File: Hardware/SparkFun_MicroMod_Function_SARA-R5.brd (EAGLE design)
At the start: 37.5 x 65 mm, 120 parts, among them J1 MICROMOD_FUNCTION_STANDARD, J2 U.FL, J4 U.FL, J9 NANO_SIM, Q2 310mA/60V/1.6Ω, Q3 310mA/60V/1.6Ω, Q5 310mA/60V/1.6Ω, Q6 310mA/60V/1.6Ω, U1 SARA-R510M8S, U11 74HC1G04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

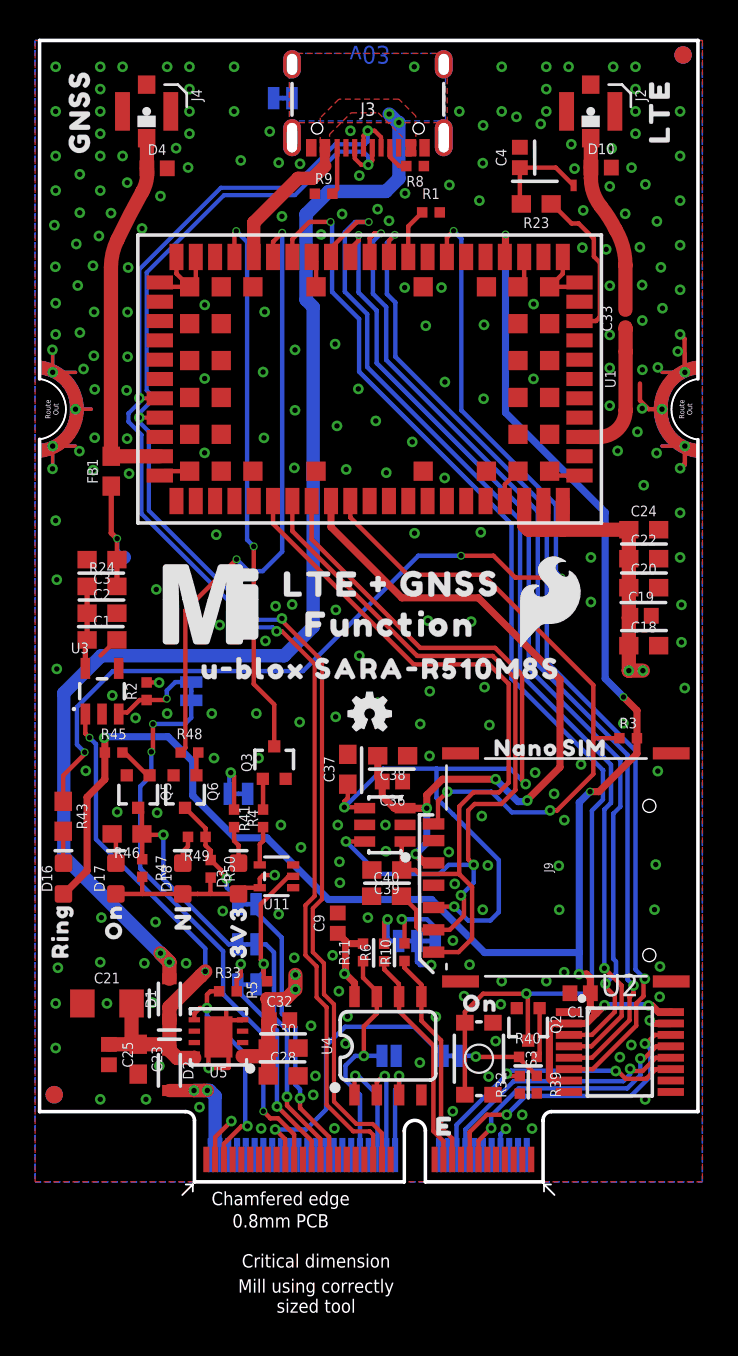
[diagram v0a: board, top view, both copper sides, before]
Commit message: ESD diode on D+ and D- USB lines
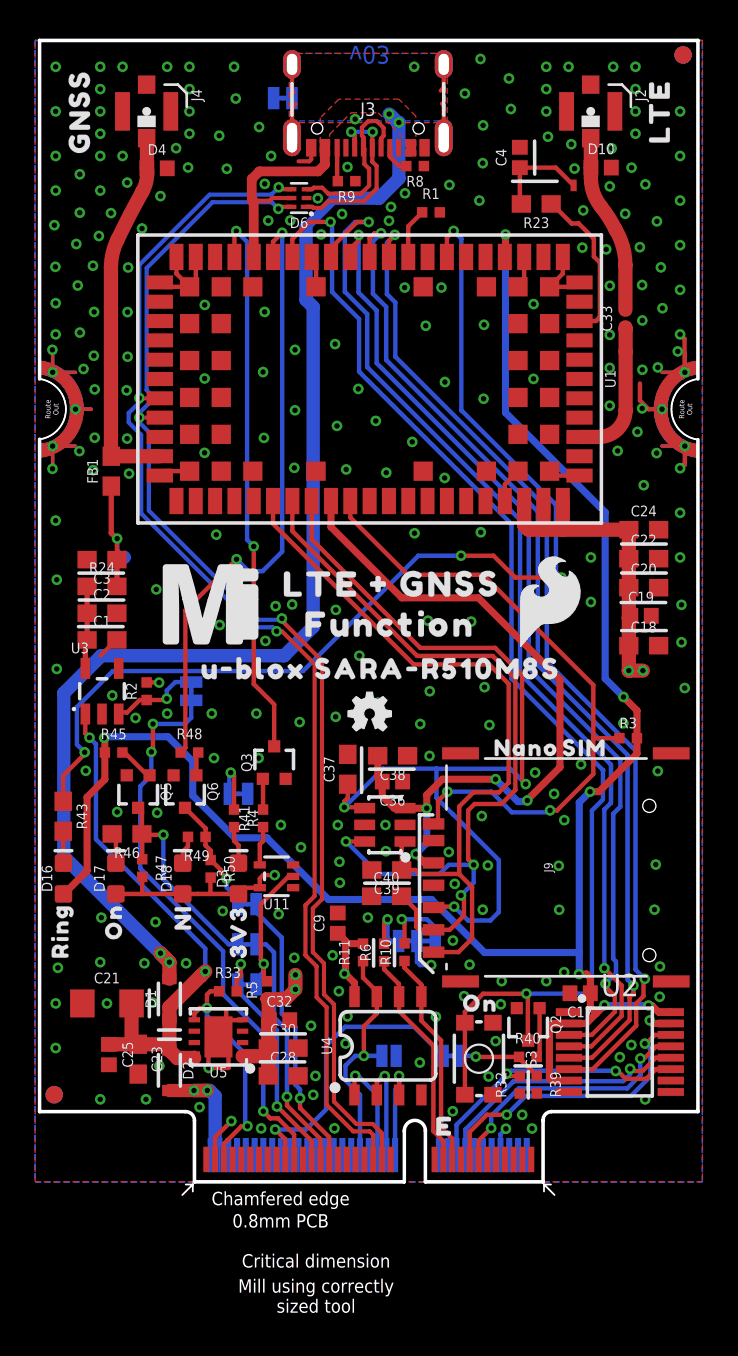
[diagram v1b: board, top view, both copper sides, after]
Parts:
- added D6: PRTR5V0U2F, SparkFun-IC-Power:SOT886
- moved R9 1.49 mm to (17.7, 57.0), turned to 180 degrees
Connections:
- new net N$10: D6.1, J3.A6, J3.B6
- new net N$15: D6.3, J3.A7, J3.B7
- net GND: now also D6.2
- net USB_N: now also D6.4; no longer J3.A7, J3.B7
- net USB_P: now also D6.6; no longer J3.A6, J3.B6
- net V_USB: now also D6.5
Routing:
- net N$15: track 0.00 -> 10.2 mm
- net N$10: track 0.00 -> 10.0 mm, vias 0 -> 2
- net USB_N: track 78.9 -> 70.4 mm
- net USB_P: track 78.3 -> 69.9 mm
- net SHLD: track 0.00 -> 7.17 mm
- net V_USB: track 77.4 -> 80.8 mm
- net GND: track 39.2 -> 40.6 mm, vias 251 -> 254
- net N$5: track 2.73 -> 1.92 mm

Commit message: RF traces corrected to 12.3mil
-also updated calc paragraph in SCH
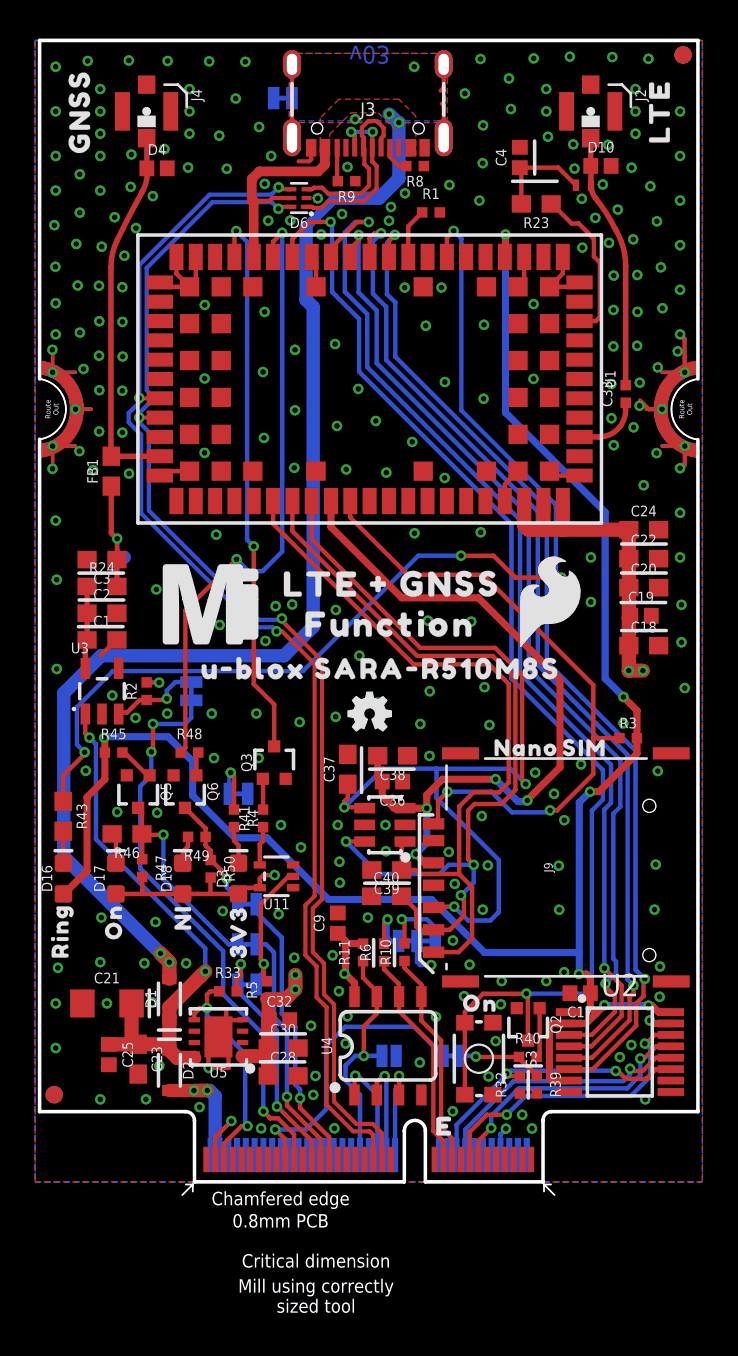
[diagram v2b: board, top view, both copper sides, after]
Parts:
- moved C33 4.29 mm to (33.6, 44.9)
- moved L2 0.13 mm to (31.2, 56.8)
- moved D10 0.09 mm to (32.2, 57.9)
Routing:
- net LTE_ANT: track 8.07 -> 3.69 mm
- net N$11: track 11.3 -> 14.5 mm
- net GND: track 40.6 -> 39.6 mm, vias 254 -> 258
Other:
- board text added: "0.8mm PCB ENIG Finish 45 degree chamfered edge 4-layer Board Soldermask Color: red"
- board text removed: "0.8mm PCB ENIG Finish 45 degree chamfered edge 2-layer Board Soldermask Color: red"

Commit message: LED disable jumpers added
-LTE_RI_LED, LTE_NI_LED, LTE_ON
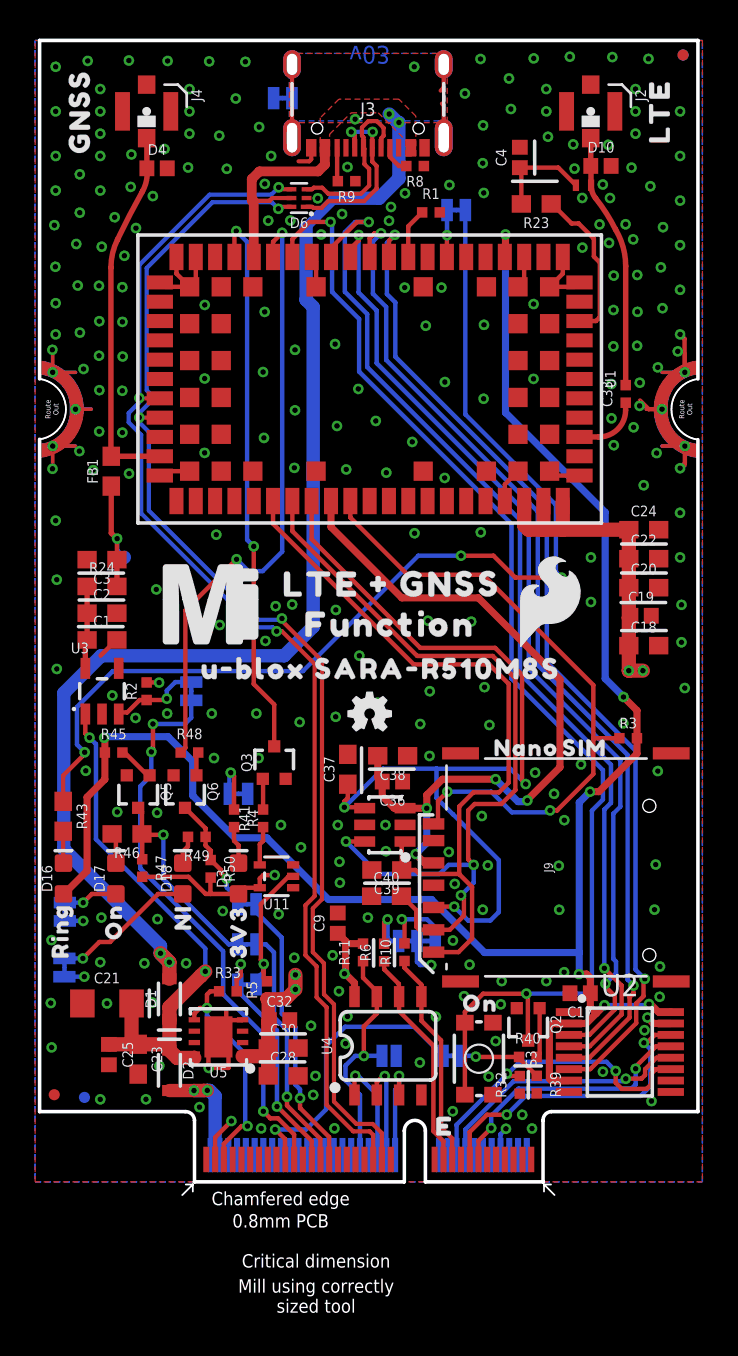
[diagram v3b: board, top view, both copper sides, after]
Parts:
- added LTE_NI_LED, LTE_ON_LED, LTE_RI_LED: JUMPER-SMT_2_NC_TRACE_SILK, SparkFun-Jumpers:SMT-JUMPER_2_NC_TRACE_SILK
- added U$22: (no value), output:#LTE_RI_LED#0
- added U$23: (no value), output:#LTE_RST#0
- added U$24: (no value), output:#LTE_ON_LED#0
- FD1, FD2, FD3, FD4: value FIDUCIAL1X2 -> FIDUCIALUFIDUCIAL; device SparkFun-Aesthetics:FIDUCIAL-1X2 -> SparkFun-Aesthetics:FIDUCIAL-MICRO
- U$9: device output:#LTE_RESET#0 -> output:#NI_LED#0
- moved U$9 3.41 mm to (1.66, 7.95), turned to 90 degrees
- moved FD2 1.73 mm to (2.81, 4.81)
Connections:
- new net N$19: D18.A, LTE_NI_LED.1
- new net N$20: LTE_RI_LED.1, R43.1
- new net N$21: D17.A, LTE_ON_LED.1
- net 3.3V: now also LTE_NI_LED.2, LTE_ON_LED.2; no longer D17.A, D18.A
- net LTE_18_RI: now also LTE_RI_LED.2; no longer R43.1
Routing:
- net N$20: track 0.00 -> 60.9 mm, vias 0 -> 3
- net LTE_18_RI: track 61.7 -> 2.68 mm, vias 4 -> 1
- net N$19: track 0.00 -> 8.26 mm, vias 0 -> 1
- net N$21: track 0.00 -> 3.11 mm, vias 0 -> 1
- net CTS: track 16.5 -> 18.1 mm
- net 3.3V: track 49.9 -> 50.2 mm, vias 8 -> 10
- net GND: vias 258 -> 259

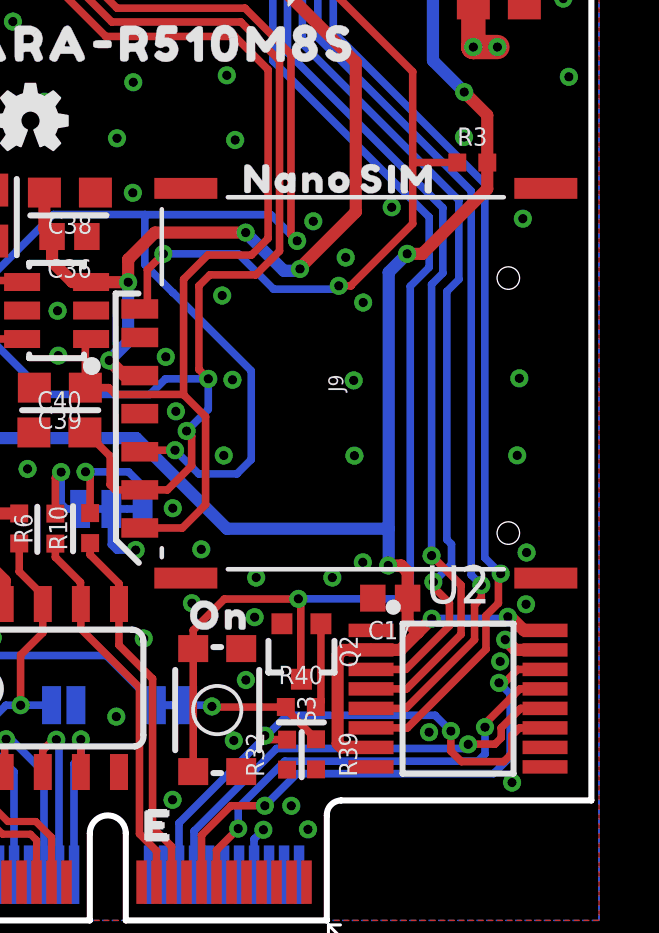
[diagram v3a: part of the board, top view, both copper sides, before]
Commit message: add 0.1uF cap on VCCB for level shifter
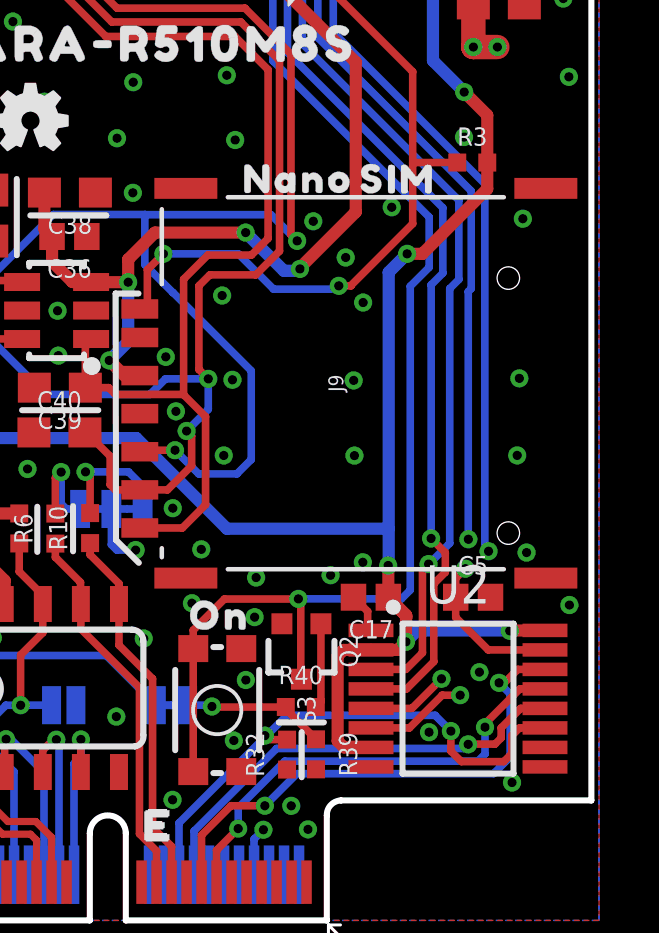
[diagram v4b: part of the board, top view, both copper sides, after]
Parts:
- added C5: 0.1uF, SparkFun-Capacitors:0402
- moved C17 0.64 mm to (30.4, 10.8)
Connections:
- net 3.3V: now also C5.1
- net GND: now also C5.2
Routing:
- net 3.3V: track 50.2 -> 53.9 mm
- net GND: track 39.6 -> 41.0 mm
- net LTE_18_TXI: track 55.7 -> 55.1 mm
- net LTE_18_CTS: track 57.3 -> 57.2 mm, vias 2 -> 3
- net LTE_18_RTS: vias 2 -> 3

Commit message: Library work and BOM consolidation
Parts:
- C17, C19, C25, C32, C36, C5, C9: device SparkFun-Capacitors:0402 -> SparkFun-Capacitors:0402-TIGHT
- C2: device SparkFun-Capacitors:0603 -> SparkFun-Capacitors:0402-TIGHT
- C24: device HPG_Solution:0603 -> SparkFun-Capacitors:0603
- J9: device HPG_Solution_v1.0:NANO_SIM_PP -> SparkFun-Connectors:NANO_SIM_PP
- R23: device SparkFun-Resistors:0603 -> SparkFun-Resistors:0402-TIGHT
- moved C36 0.41 mm to (19.9, 22.8)
- moved C2 0.36 mm to (3.45, 32.4)
- moved C19 0.10 mm to (34.4, 32.2)
- moved C32 0.08 mm to (13.8, 9.21)
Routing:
- net 3.3V: track 53.9 -> 54.8 mm
- net VCCIO: track 106.4 -> 105.6 mm

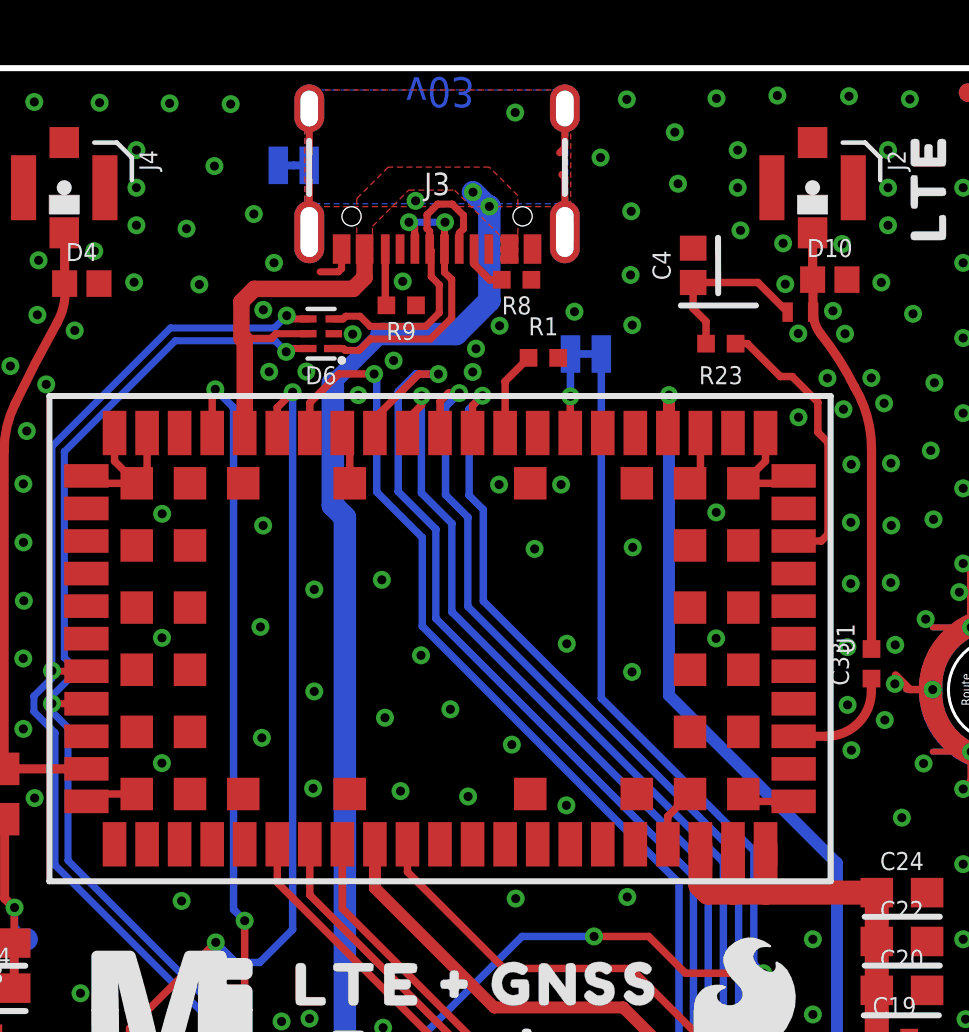
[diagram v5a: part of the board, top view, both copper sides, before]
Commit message: added PTC fuse to USB input
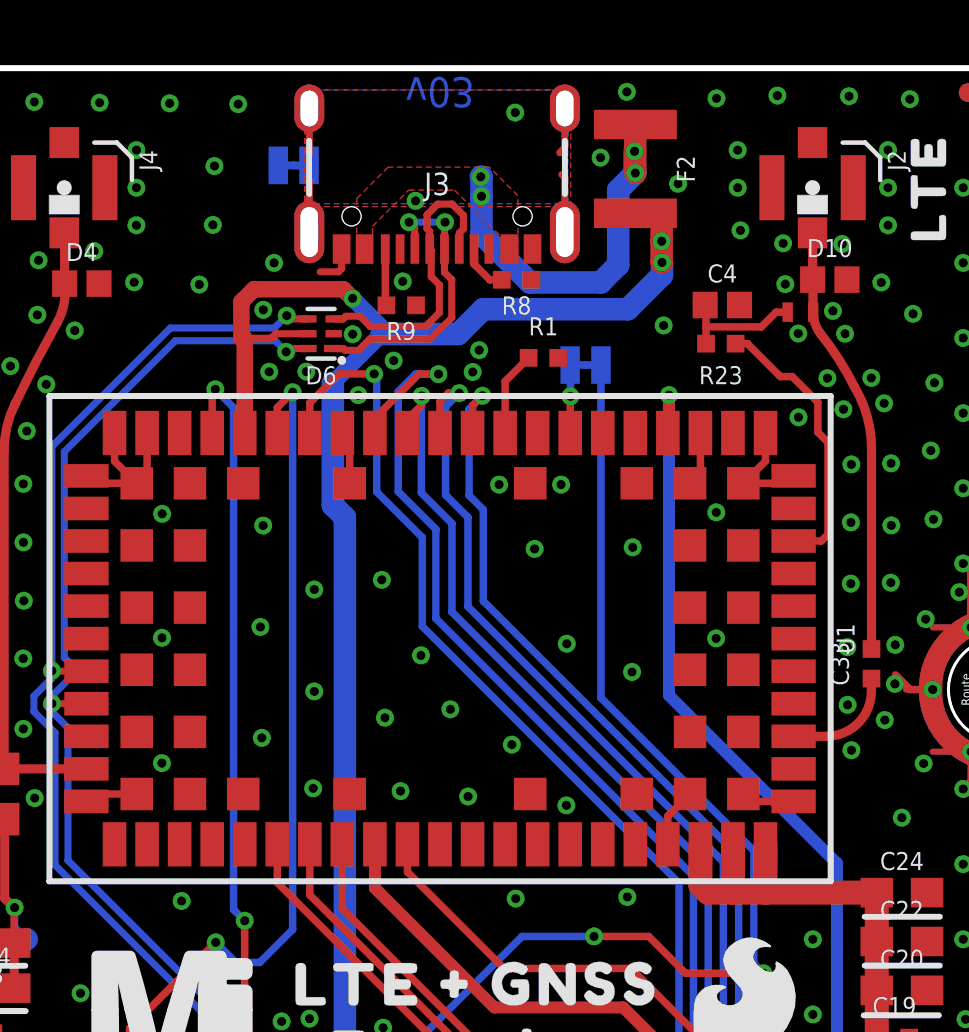
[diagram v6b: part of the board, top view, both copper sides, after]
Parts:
- added F2: 6V/2A, SparkFun-Fuses:1210
- moved C4 1.66 mm to (28.6, 57.0), turned to 0 degrees
- moved LTE_RI_LED 0.38 mm to (24.0, 55.0)
- moved U$22 0.27 mm to (30.3, 55.0)
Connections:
- new net N$22: F2.1, J3.VBUS1, J3.VBUS2
- net V_USB: now also F2.2; no longer J3.VBUS1, J3.VBUS2
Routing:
- net N$22: track 0.00 -> 13.2 mm, vias 0 -> 4
- net V_USB: track 80.8 -> 86.8 mm, vias 4 -> 5
- net N$18: track 5.85 -> 4.28 mm
- net GND: vias 259 -> 253
- added copper zone on layer 1, net N$22
- added copper zone on layer 16, net V_USB
- removed copper zone on layer 1, net V_USB
